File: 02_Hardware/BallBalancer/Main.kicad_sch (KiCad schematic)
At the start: 51 parts, among them J1 ENCODER1_CON, J2 ENCODER2_CON, J3 USB_B_Micro, J4 SWD, J5 Conn_01x03_Pin, J7 Conn_01x03_Pin, J8 Conn_01x03_Pin, U1 STM32L412K8Tx, U2 USBLC6-2SC6

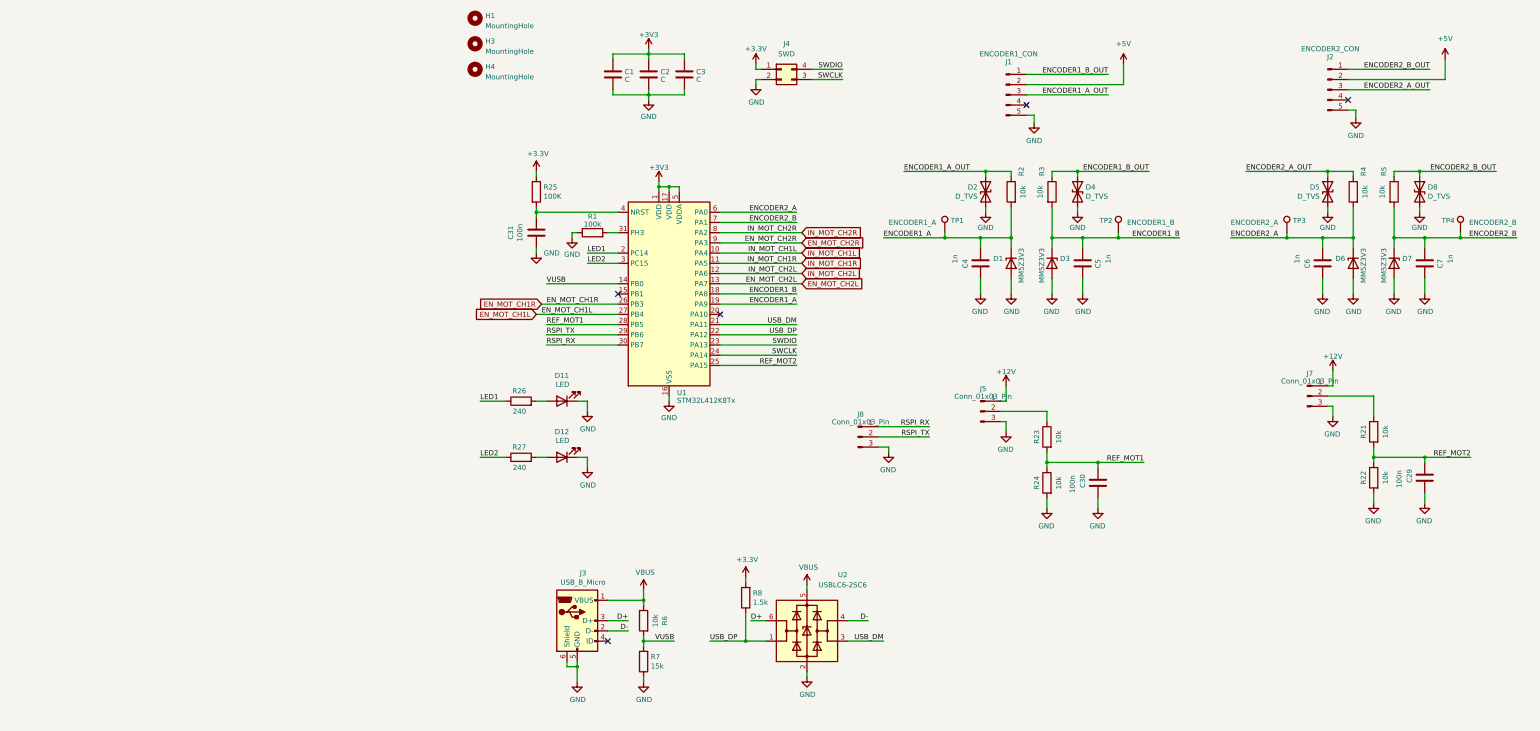
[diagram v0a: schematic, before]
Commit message: ERC and DRC warnings and errors in schema and layout fixed
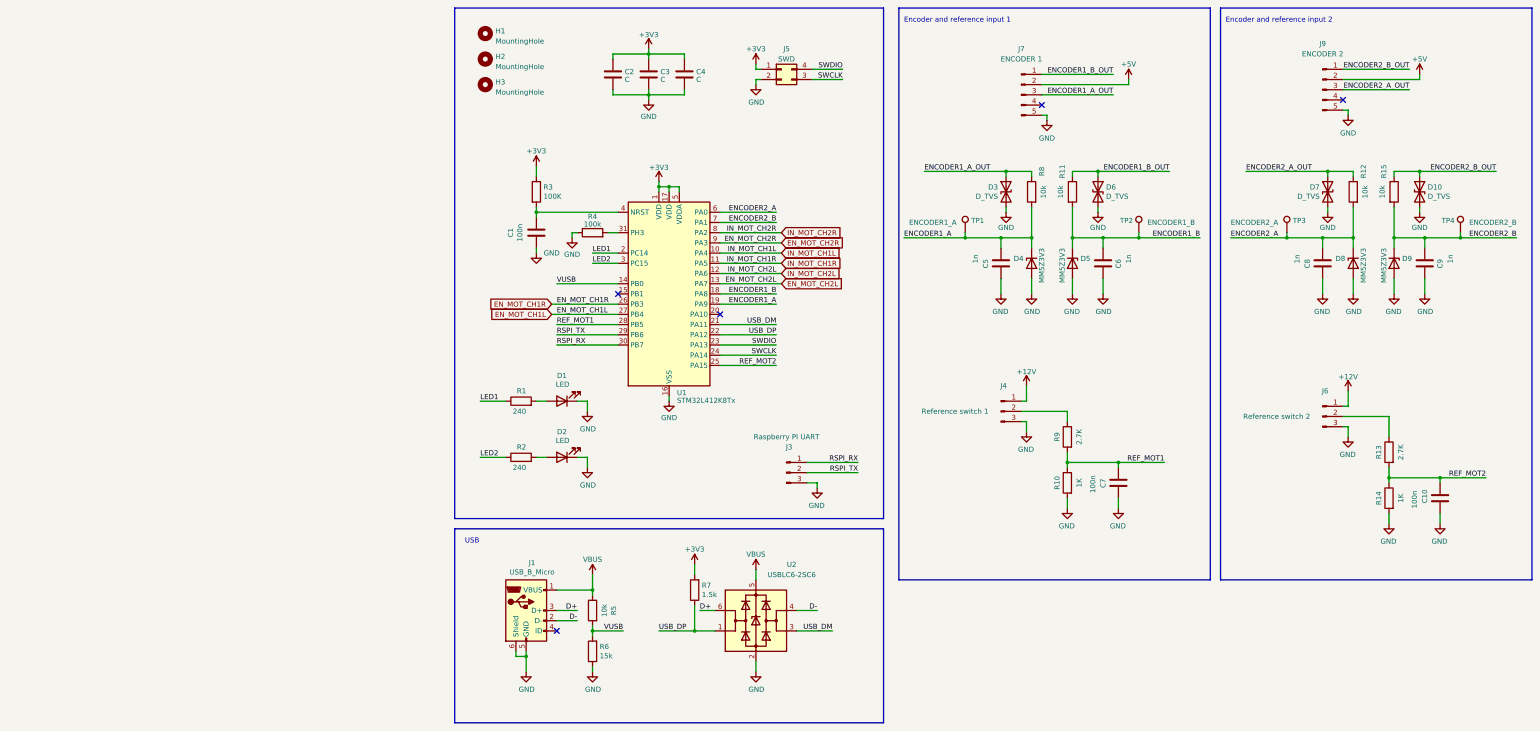
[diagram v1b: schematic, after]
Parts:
- removed J1: ENCODER1_CON, Connector_PinHeader_2.54mm:PinHeader_1x05_P2.54mm_Vertical, symbol Connector:Conn_01x05_Male
- removed J2: ENCODER2_CON, Connector_PinHeader_2.54mm:PinHeader_1x05_P2.54mm_Vertical, symbol Connector:Conn_01x05_Male
- removed J4: SWD, Connector_PinHeader_2.54mm:PinHeader_2x02_P2.54mm_Vertical, symbol Connector_Generic:Conn_02x02_Counter_Clockwise
- added J5: SWD, Connector_PinHeader_2.54mm:PinHeader_2x02_P2.54mm_Vertical, symbol Connector_Generic:Conn_02x02_Counter_Clockwise
- added J7: ENCODER 1, Connector_PinHeader_2.54mm:PinHeader_1x05_P2.54mm_Vertical, symbol Connector:Conn_01x05_Pin
- added J9: ENCODER 2, Connector_PinHeader_2.54mm:PinHeader_1x05_P2.54mm_Vertical, symbol Connector:Conn_01x05_Pin
- J3: renamed from J8; value Conn_01x03_Pin -> Raspberry PI UART
- J4: renamed from J5; value Conn_01x03_Pin -> Reference switch 1
- J6: renamed from J7; value Conn_01x03_Pin -> Reference switch 2
- R10: renamed from R24; value 10k -> 1K; Hersteller Nr. RT0603FRE0710KL -> (none); Mouser Nr. 603-RT0603FRE0710KL -> (none)
- R13: renamed from R21; value 10k -> 2.7K; Hersteller Nr. RT0603FRE0710KL -> (none); Mouser Nr. 603-RT0603FRE0710KL -> (none)
- R14: renamed from R22; value 10k -> 1K; Hersteller Nr. RT0603FRE0710KL -> (none); Mouser Nr. 603-RT0603FRE0710KL -> (none)
- R9: renamed from R23; value 10k -> 2.7K; Hersteller Nr. RT0603FRE0710KL -> (none); Mouser Nr. 603-RT0603FRE0710KL -> (none)
- renumbered C31 to C1, C29 to C10, C1 to C2, C2 to C3, C3 to C4, C4 to C5, C5 to C6, C30 to C7, C6 to C8, C7 to C9, D11 to D1, D8 to D10, D12 to D2, D2 to D3, D1 to D4, D3 to D5, D4 to D6, D5 to D7, D6 to D8, D7 to D9, H3 to H2, H4 to H3, J3 to J1, R26 to R1, R3 to R11, R4 to R12, R5 to R15, R27 to R2, R25 to R3, R1 to R4, R6 to R5, R7 to R6, R8 to R7, R2 to R8
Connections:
- net +3V3: now also J5.1 (Pin_1)
- net +5V: now also J7.2 (Pin_2), J9.2 (Pin_2)
- net ENCODER1_A_OUT: now also J7.3 (Pin_3)
- net ENCODER1_B_OUT: now also J7.1 (Pin_1)
- net ENCODER2_A_OUT: now also J9.3 (Pin_3)
- net ENCODER2_B_OUT: now also J9.1 (Pin_1)
- net GND: now also J5.2 (Pin_2), J7.5 (Pin_5), J9.5 (Pin_5)
- net SWCLK: now also J5.3 (Pin_3)
- net SWDIO: now also J5.4 (Pin_4)
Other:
- note added: "Encoder and reference input 1"
- note added: "Encoder and reference input 2"
- note added: "USB"
- moved on the sheet: C10, C5, C6, C7, D3, D4, D5, D6, H1, H2, H3, J1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

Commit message: Test points added and BOM created
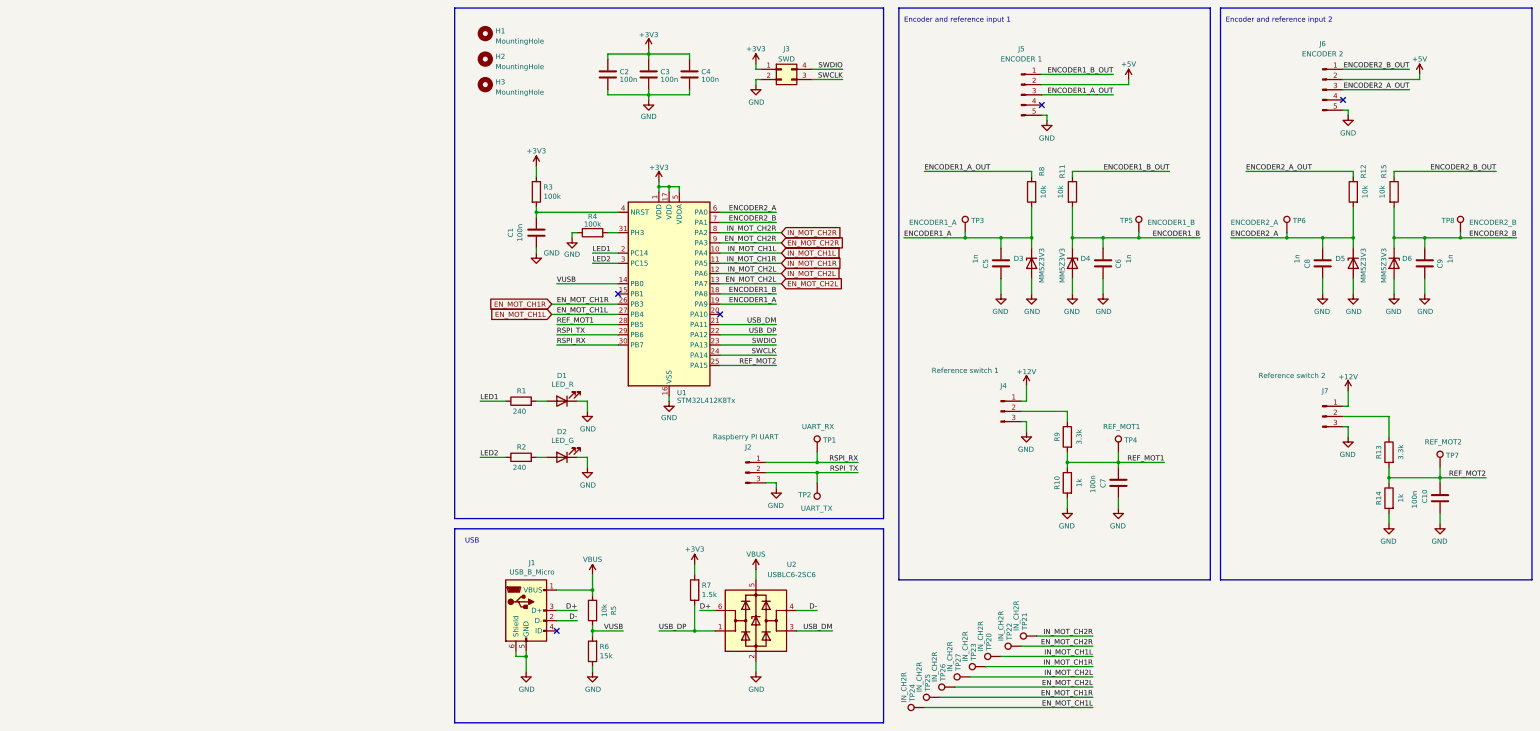
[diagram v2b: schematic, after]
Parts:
- removed D10, D3, D6, D7: D_TVS, Diode_SMD:D_0603_1608Metric, symbol Device:D_TVS
- added TP1: UART_RX, TestPoint:TestPoint_Pad_D1.0mm, symbol Connector:TestPoint
- added TP2: UART_TX, TestPoint:TestPoint_Pad_D1.0mm, symbol Connector:TestPoint
- added TP20, TP21, TP22, TP23, TP24, TP25, TP26, TP27: IN_CH2R, TestPoint:TestPoint_Pad_D1.0mm, symbol Connector:TestPoint
- added TP4: REF_MOT1, TestPoint:TestPoint_Pad_D1.0mm, symbol Connector:TestPoint
- added TP7: REF_MOT2, TestPoint:TestPoint_Pad_D1.0mm, symbol Connector:TestPoint
- C1: Hersteller Nr. CL10B104KB8NNWC -> 885382206004; Info (none) -> 0.1uF; 50V, X7R; -55C;+125C; Mouser Nr. 187-CL10B104KB8NNWC -> 710-885382206004
- C10, C7: Hersteller Nr. (none) -> 885382206004; Info (none) -> 0.1uF; 50V, X7R; -55C;+125C; Mouser Nr. (none) -> 710-885382206004
- C2, C3, C4: value C -> 100n; Hersteller Nr. (none) -> 885382206004; Info (none) -> 0.1uF; 50V, X7R; -55C;+125C; Mouser Nr. (none) -> 710-885382206004
- C5, C6, C8, C9: Info (none) -> 1nF; 50V; X7R; -55C;+125C
- D1: value LED -> LED_R; Hersteller Nr. 150060VS75000 -> 150060RS75000; Info (none) -> Red; 20mA; 2V; Mouser Nr. 710-150060VS75000 -> 710-150060RS75000
- D2: value LED -> LED_G; Info (none) -> Green; 20mA; 2V
- D3: renamed from D4; Info (none) -> 3.3V; 500mW; Mouser Nr. 863-MM5Z3V3T1G -> 863-MM5Z3V3T1G
- D4: renamed from D5; Info (none) -> 3.3V; 500mW; Mouser Nr. 863-MM5Z3V3T1G -> 863-MM5Z3V3T1G
- D5: renamed from D8; Info (none) -> 3.3V; 500mW; Mouser Nr. 863-MM5Z3V3T1G -> 863-MM5Z3V3T1G
- D6: renamed from D9; Info (none) -> 3.3V; 500mW; Mouser Nr. 863-MM5Z3V3T1G -> 863-MM5Z3V3T1G
- H1, H2, H3: now left out of the parts list
- J1: Hersteller Nr. (none) -> UJ2-MBH-1-SMT-TR; Info (none) -> USB Mini B; Mouser Nr. (none) -> 490-UJ2-MBH-1-SMT
- J5: renamed from J7; Info (none) -> Connector for AMT102 Encoder (AMT102-V)
- J6: renamed from J9; Info (none) -> Connector for AMT102 Encoder (AMT102-V)
- R1, R2: Info (none) -> 75V; 1%; 100mW; -55C; +155C
- R10, R14: value 1K -> 1k; Hersteller Nr. (none) -> CRCW06031K00FKEAC; Info (none) -> 75V; 1%; 100mW; -55C; +155C; Mouser Nr. (none) -> 71-CRCW06031K00FKEAC
- R11, R12, R15, R5, R8: Hersteller Nr. RT0603FRE0710KL -> CRCW060310K0FKEAC; Info (none) -> 75V; 1%; 100mW; -55C; +155C; Mouser Nr. 603-RT0603FRE0710KL -> 71-CRCW060310K0FKEAC
- R13, R9: value 2.7K -> 3.3k; Hersteller Nr. (none) -> ERJ-PB3B3301V; Info (none) -> 75V; 0.1%; 200mW; -55C; +155C; Mouser Nr. (none) -> 667-ERJ-PB3B3301V
- R3: value 100K -> 100k; Info (none) -> 75V; 1%; 100mW; -55C; +155C
- R4: Hersteller Nr. (none) -> CRCW0603100KFKEAC; Info (none) -> 75V; 1%; 100mW; -55C; +155C; Mouser Nr. (none) -> 71-CRCW0603100KFKEAC
- R6: Hersteller Nr. RT0603BRB0715KL -> ERJ-3EKF1502V; Info (none) -> 75V; 1%; 100mW; -55C; +155C; Mouser Nr. 603-RT0603BRB0715KL -> 667-ERJ-3EKF1502V
- R7: Hersteller Nr. RT0603FRE101K5L -> CRCW06031K50JNEAC; Info (none) -> 75V; 5%; 100mW; -55C; +155C; Mouser Nr. 603-RT0603FRE101K5L -> 71-CRCW06031K50JNEAC
- U1: Hersteller Nr. (none) -> STM32L412K8T6; Info (none) -> 80MHz; 40kB RAM; 64 kB Flash; Mouser Nr. (none) -> 511-STM32L412K8T6
- U2: Info (none) -> USB TVS
- renumbered J3 to J2, J5 to J3, J6 to J7, TP1 to TP3, TP2 to TP5, TP3 to TP6, TP4 to TP8
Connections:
- net EN_MOT_CH1L: now also TP24.1
- net EN_MOT_CH1R: now also TP25.1
- net EN_MOT_CH2L: now also TP26.1
- net EN_MOT_CH2R: now also TP22.1
- net IN_MOT_CH1L: now also TP20.1
- net IN_MOT_CH1R: now also TP23.1
- net IN_MOT_CH2L: now also TP27.1
- net IN_MOT_CH2R: now also TP21.1
- net REF_MOT1: now also TP4.1
- net REF_MOT2: now also TP7.1
- net RSPI_RX: now also TP1.1
- net RSPI_TX: now also TP2.1
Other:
- moved on the sheet: C2, C4, J2

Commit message: CAD files and hardware manufacturing data added
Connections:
- net EN_MOT_CH2R: now also U1.10 (PA4); no longer U1.9 (PA3)
- net IN_MOT_CH1L: now also U1.9 (PA3); no longer U1.10 (PA4)
- net IN_MOT_CH1R: now also U1.20 (PA10); no longer U1.11 (PA5)
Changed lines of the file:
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@@
   (no_connect (at 39.37 170.18))
   (no_connect (at 234.95 38.1))
-  (no_connect (at 80.01 91.44))
+  (no_connect (at 80.01 78.74))
   (wire (pts (xy 130.81 55.88) (xy 157.48 55.88))
     (stroke (width 0) (type default))
@@
     (stroke (width 0) (type default))
   )
+  (wire (pts (xy 80.01 73.66) (xy 95.25 73.66))
+    (stroke (width 0) (type default))
+  )
+  (wire (pts (xy 44.45 71.12) (xy 43.18 71.12))
+    (stroke (width 0) (type default))
+  )
+  (wire (pts (xy 104.14 125.73) (xy 104.14 128.27))
+    (stroke (width 0) (type default))
+  )
+  (wire (pts (xy 160.02 34.29) (xy 181.61 34.29))
+    (stroke (width 0) (type default))
+  )
+  (wire (pts (xy 259.08 132.08) (xy 270.51 132.08))
+    (stroke (width 0) (type default))
+  )
+  (wire (pts (xy 52.07 71.12) (xy 54.61 71.12))
+    (stroke (width 0) (type default))
+  )
+  (wire (pts (xy 157.48 86.36) (xy 157.48 82.55))
+    (stroke (width 0) (type default))
+  )
+  (wire (pts (xy 149.86 72.39) (xy 149.86 74.93))
+    (stroke (width 0) (type default))
+  )
+  (wire (pts (xy 38.1 88.9) (xy 54.61 88.9))
+    (stroke (width 0) (type default))
+  )
+  (wire (pts (xy 156.21 113.03) (xy 154.94 113.03))
+    (stroke (width 0) (type default))
+  )
+  (wire (pts (xy 48.26 170.18) (xy 48.26 171.45))
+    (stroke (width 0) (type default))
+  )
+  (wire (pts (xy 179.07 137.16) (xy 179.07 139.7))
+    (stroke (width 0) (type default))
+  )
+  (wire (pts (xy 80.01 96.52) (xy 93.98 96.52))
+    (stroke (width 0) (type default))
+  )
+  (wire (pts (xy 237.49 57.15) (xy 237.49 55.88))
+    (stroke (width 0) (type default))
+  )
+  (wire (pts (xy 234.95 116.84) (xy 246.38 116.84))
+    (stroke (width 0) (type default))
+  )
+  (wire (pts (xy 220.98 72.39) (xy 207.01 72.39))
+    (stroke (width 0) (type default))
+  )
+  (wire (pts (xy 72.39 26.67) (xy 72.39 27.94))
+    (stroke (width 0) (type default))
+  )
+  (wire (pts (xy 93.98 133.35) (xy 93.98 134.62))
+    (stroke (width 0) (type default))
+  )
+  (wire (pts (xy 99.06 170.18) (xy 107.95 170.18))
+    (stroke (width 0) (type default))
+  )
+  (wire (pts (xy 88.9 30.48) (xy 90.17 30.48))
+    (stroke (width 0) (type default))
+  )
+  (wire (pts (xy 52.07 35.56) (xy 52.07 36.83))
+    (stroke (width 0) (type default))
+  )
+  (wire (pts (xy 80.01 91.44) (xy 95.25 91.44))
+    (stroke (width 0) (type default))
+  )
+  (wire (pts (xy 62.23 25.4) (xy 62.23 26.67))
+    (stroke (width 0) (type default))
+  )
+  (wire (pts (xy 167.64 72.39) (xy 175.26 72.39))
+    (stroke (width 0) (type default))
+  )
+  (wire (pts (xy 67.31 111.76) (xy 67.31 113.03))
+    (stroke (width 0) (type default))
+  )
+  (wire (pts (xy 156.21 109.22) (xy 156.21 113.03))
+    (stroke (width 0) (type default))
+  )
+  (wire (pts (xy 229.87 72.39) (xy 229.87 74.93))
+    (stroke (width 0) (type default))
+  )
+  (wire (pts (xy 80.01 88.9) (xy 93.98 88.9))
+    (stroke (width 0) (type default))
+  )
+  (wire (pts (xy 110.49 33.02) (xy 102.87 33.02))
+    (stroke (width 0) (type default))
+  )
+  (wire (pts (xy 62.23 35.56) (xy 62.23 36.83))
+    (stroke (width 0) (type default))
+  )
   (wire (pts (xy 80.01 76.2) (xy 95.25 76.2))
     (stroke (width 0) (type default))
   )
-  (wire (pts (xy 44.45 71.12) (xy 43.18 71.12))
-    (stroke (width 0) (type default))
-  )
-  (wire (pts (xy 104.14 125.73) (xy 104.14 128.27))
-    (stroke (width 0) (type default))
-  )
-  (wire (pts (xy 160.02 34.29) (xy 181.61 34.29))
-    (stroke (width 0) (type default))
-  )
-  (wire (pts (xy 259.08 132.08) (xy 270.51 132.08))
-    (stroke (width 0) (type default))
-  )
-  (wire (pts (xy 52.07 71.12) (xy 54.61 71.12))
-    (stroke (width 0) (type default))
-  )
-  (wire (pts (xy 157.48 86.36) (xy 157.48 82.55))
-    (stroke (width 0) (type default))
-  )
-  (wire (pts (xy 149.86 72.39) (xy 149.86 74.93))
-    (stroke (width 0) (type default))
-  )
-  (wire (pts (xy 38.1 88.9) (xy 54.61 88.9))
-    (stroke (width 0) (type default))
-  )
-  (wire (pts (xy 156.21 113.03) (xy 154.94 113.03))
-    (stroke (width 0) (type default))
-  )
-  (wire (pts (xy 48.26 170.18) (xy 48.26 171.45))
-    (stroke (width 0) (type default))
-  )
-  (wire (pts (xy 179.07 137.16) (xy 179.07 139.7))
-    (stroke (width 0) (type default))
-  )
-  (wire (pts (xy 80.01 96.52) (xy 93.98 96.52))
-    (stroke (width 0) (type default))
-  )
-  (wire (pts (xy 237.49 57.15) (xy 237.49 55.88))
-    (stroke (width 0) (type default))
-  )
-  (wire (pts (xy 234.95 116.84) (xy 246.38 116.84))
-    (stroke (width 0) (type default))
-  )
-  (wire (pts (xy 220.98 72.39) (xy 207.01 72.39))
-    (stroke (width 0) (type default))
-  )
-  (wire (pts (xy 72.39 26.67) (xy 72.39 27.94))
-    (stroke (width 0) (type default))
-  )
-  (wire (pts (xy 93.98 133.35) (xy 93.98 134.62))
-    (stroke (width 0) (type default))
-  )
-  (wire (pts (xy 99.06 170.18) (xy 107.95 170.18))
-    (stroke (width 0) (type default))
-  )
-  (wire (pts (xy 88.9 30.48) (xy 90.17 30.48))
-    (stroke (width 0) (type default))
-  )
-  (wire (pts (xy 52.07 35.56) (xy 52.07 36.83))
-    (stroke (width 0) (type default))
-  )
-  (wire (pts (xy 80.01 78.74) (xy 95.25 78.74))
-    (stroke (width 0) (type default))
-  )
-  (wire (pts (xy 62.23 25.4) (xy 62.23 26.67))
-    (stroke (width 0) (type default))
-  )
-  (wire (pts (xy 167.64 72.39) (xy 175.26 72.39))
-    (stroke (width 0) (type default))
-  )
-  (wire (pts (xy 67.31 111.76) (xy 67.31 113.03))
-    (stroke (width 0) (type default))
-  )
-  (wire (pts (xy 156.21 109.22) (xy 156.21 113.03))
-    (stroke (width 0) (type default))
-  )
-  (wire (pts (xy 229.87 72.39) (xy 229.87 74.93))
-    (stroke (width 0) (type default))
-  )
-  (wire (pts (xy 80.01 88.9) (xy 93.98 88.9))
-    (stroke (width 0) (type default))
-  )
-  (wire (pts (xy 110.49 33.02) (xy 102.87 33.02))
-    (stroke (width 0) (type default))
-  )
-  (wire (pts (xy 62.23 35.56) (xy 62.23 36.83))
-    (stroke (width 0) (type default))
-  )
-  (wire (pts (xy 80.01 73.66) (xy 95.25 73.66))
-    (stroke (width 0) (type default))
-  )
   (wire (pts (xy 44.45 113.03) (xy 46.99 113.03))
     (stroke (width 0) (type default))
@@
     (effects (font (size 1.27 1.27)) (justify right bottom))
   )
-  (label "IN_MOT_CH1L" (at 93.98 76.2 180) (fields_autoplaced)
+  (label "IN_MOT_CH1L" (at 93.98 73.66 180) (fields_autoplaced)
     (effects (font (size 1.27 1.27)) (justify right bottom))
   )
@@
     (effects (font (size 1.27 1.27)) (justify right bottom))
   )
-  (label "EN_MOT_CH2R" (at 93.98 73.66 180) (fields_autoplaced)
+  (label "EN_MOT_CH2R" (at 93.98 76.2 180) (fields_autoplaced)
     (effects (font (size 1.27 1.27)) (justify right bottom))
   )
@@
     (effects (font (size 1.27 1.27)) (justify right bottom))
   )
-  (label "IN_MOT_CH1R" (at 93.98 78.74 180) (fields_autoplaced)
+  (label "IN_MOT_CH1R" (at 93.98 91.44 180) (fields_autoplaced)
     (effects (font (size 1.27 1.27)) (justify right bottom))
   )
@@
     )
   )
-  (global_label "EN_MOT_CH2R" (shape input) (at 95.25 73.66 0) (fields_autoplaced)
+  (global_label "EN_MOT_CH2R" (shape input) (at 95.25 76.2 0) (fields_autoplaced)
     (effects (font (size 1.27 1.27)) (justify left))
-    (property "Intersheetrefs" "${INTERSHEET_REFS}" (at 111.4 73.66 0)
+    (property "Intersheetrefs" "${INTERSHEET_REFS}" (at 111.4 76.2 0)
       (effects (font (size 1.27 1.27)) (justify left) hide)
     )
@@
     )
   )
-  (global_label "IN_MOT_CH1R" (shape input) (at 95.25 78.74 0) (fields_autoplaced)
+  (global_label "IN_MOT_CH1R" (shape input) (at 95.25 91.44 0) (fields_autoplaced)
     (effects (font (size 1.27 1.27)) (justify left))
-    (property "Intersheetrefs" "${INTERSHEET_REFS}" (at 110.8558 78.74 0)
+    (property "Intersheetrefs" "${INTERSHEET_REFS}" (at 110.8558 91.44 0)
       (effects (font (size 1.27 1.27)) (justify left) hide)
     )
@@
     )
   )
-  (global_label "IN_MOT_CH1L" (shape input) (at 95.25 76.2 0) (fields_autoplaced)
+  (global_label "IN_MOT_CH1L" (shape input) (at 95.25 73.66 0) (fields_autoplaced)
     (effects (font (size 1.27 1.27)) (justify left))
-    (property "Intersheetrefs" "${INTERSHEET_REFS}" (at 110.6139 76.2 0)
+    (property "Intersheetrefs" "${INTERSHEET_REFS}" (at 110.6139 73.66 0)
       (effects (font (size 1.27 1.27)) (justify left) hide)
     )
